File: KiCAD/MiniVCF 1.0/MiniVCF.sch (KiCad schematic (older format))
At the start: 63 parts, among them J10 CV2, J11 CTRL_PANEL_CONN2, J12 MAIN_BOARD_CONN2, J3 AudioIn, J4 CV1, J5 AudioOut, J8 MAIN_BOARD_CONN, J9 CTRL_PANEL_CONN, U1 TL074, U2 TL074

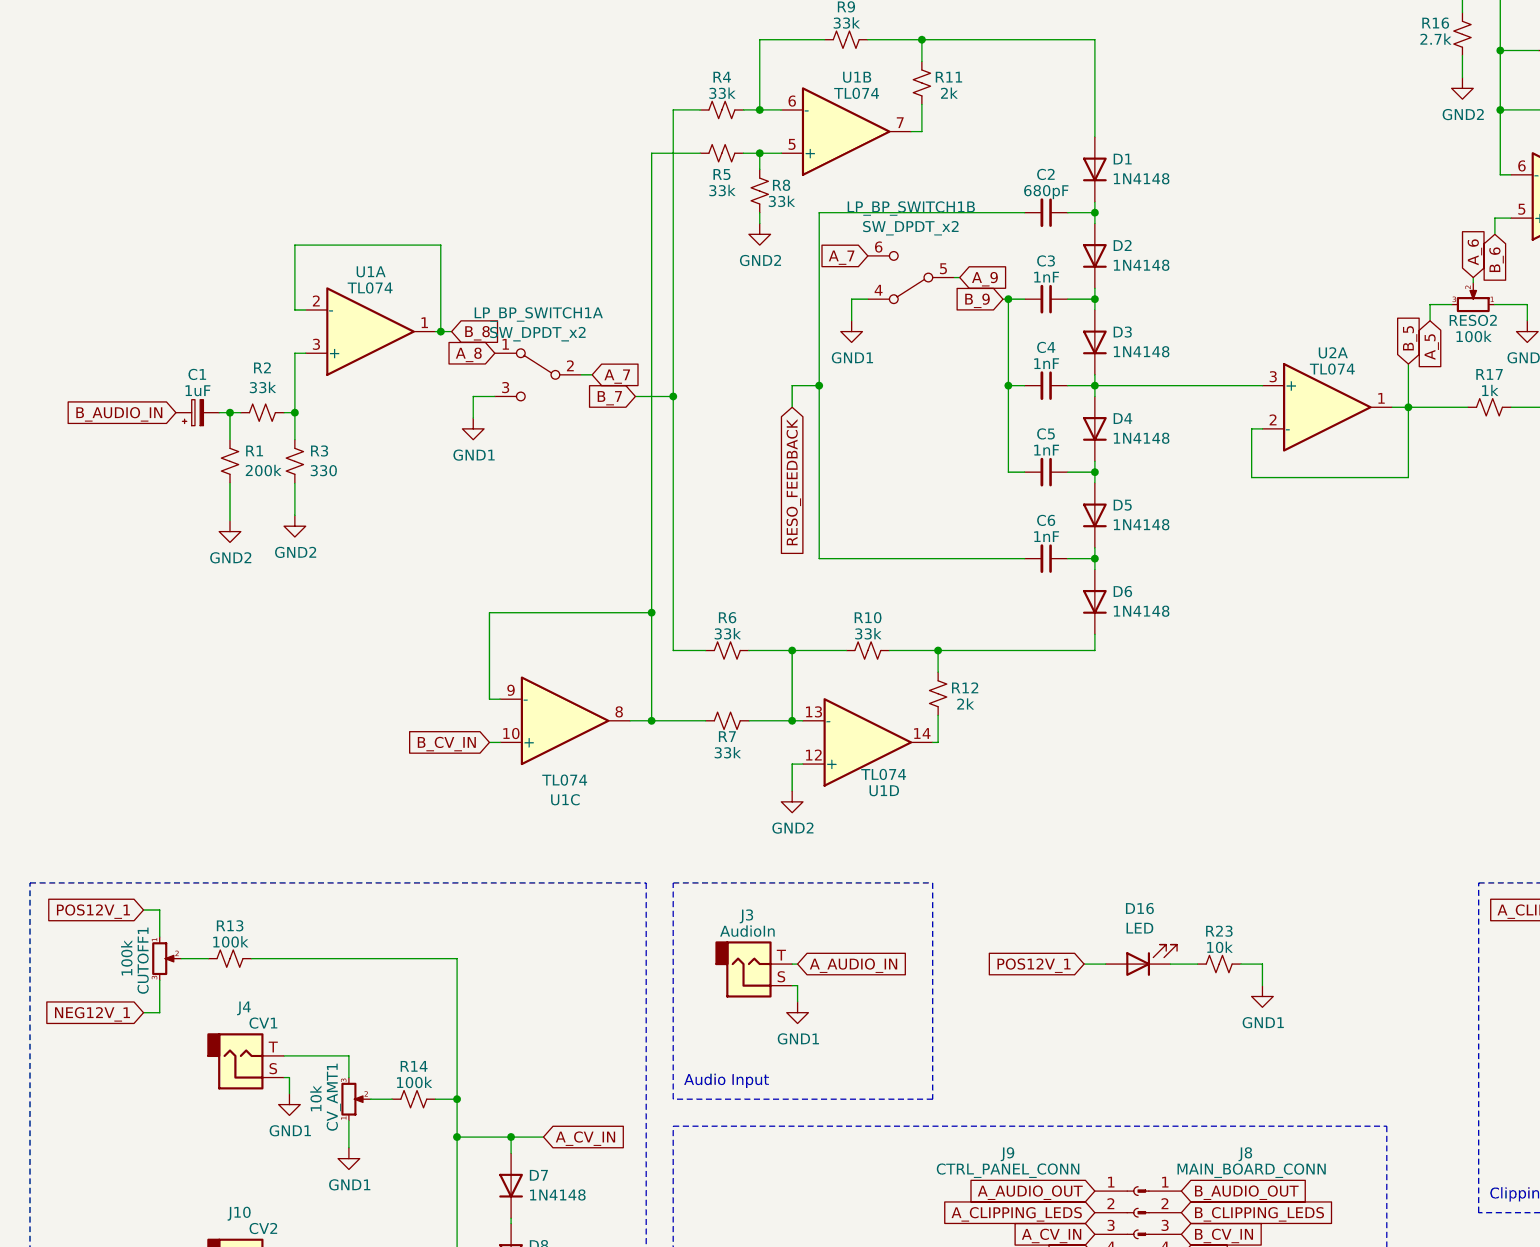
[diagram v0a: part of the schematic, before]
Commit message: Fixed toggle switch connections
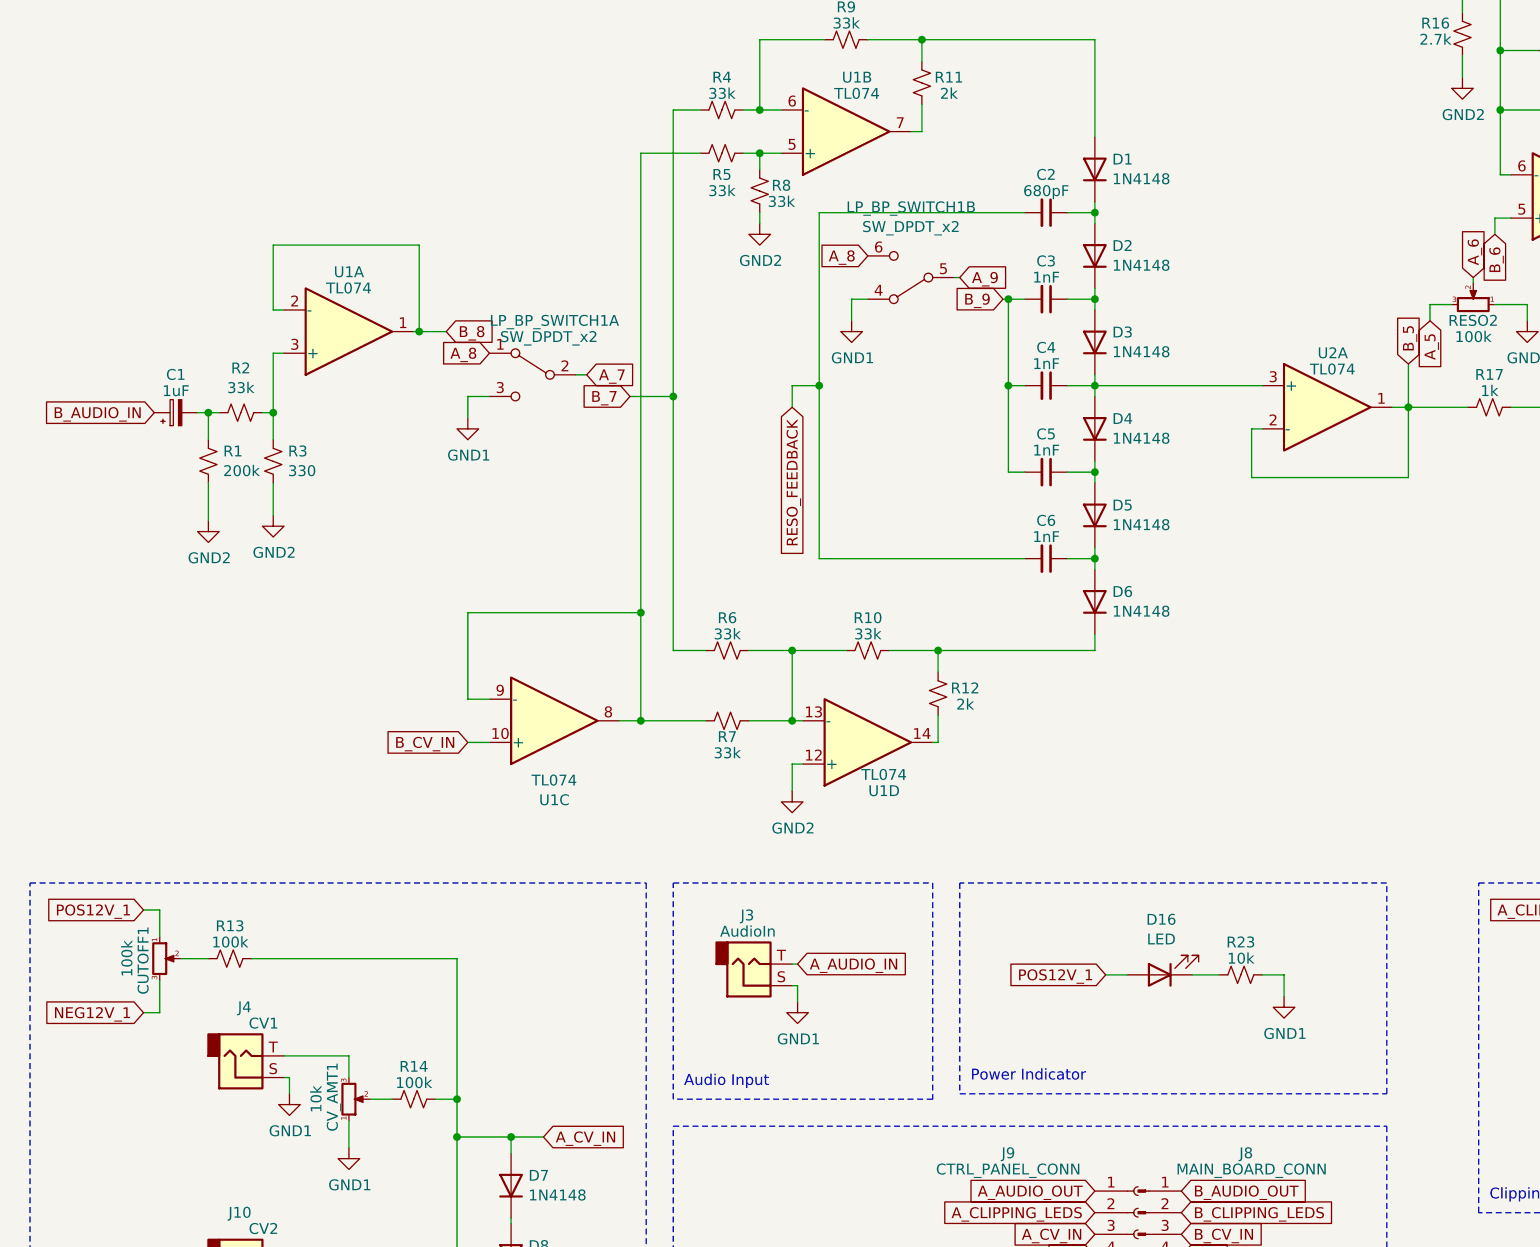
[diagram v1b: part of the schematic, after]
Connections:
- net A_7: no longer LP_BP_SWITCH1.6 (C)
- net A_8: now also LP_BP_SWITCH1.6 (C)
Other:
- note added: "Power Indicator\n"
- moved on the sheet: C1, D16, LP_BP_SWITCH1A, R1, R2, R23, R3, U1A, U1C

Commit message: Added fab files for v1.0
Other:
- moved on the sheet: R16
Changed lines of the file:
@@
 	7550 2275 7550 2350
 Wire Wire Line
-	7425 1375 7425 1675
-Wire Wire Line
-	7425 1675 7475 1675
+	7400 1375 7400 1675
+Wire Wire Line
+	7400 1675 7475 1675
 Wire Wire Line
 	8125 1375 8125 1775
@@
 Wire Wire Line
 	8125 1775 8225 1775
-Wire Wire Line
-	7425 800  7425 1100
-Connection ~ 7425 1375
+Connection ~ 7400 1375
 Wire Wire Line
 	8125 800  8125 1100
 Connection ~ 8125 1375
-Connection ~ 7425 1100
-Wire Wire Line
-	7425 1100 7425 1375
 Connection ~ 8125 1100
 Wire Wire Line
 	8125 1100 8125 1375
 Wire Wire Line
-	7250 800  7250 925
-Connection ~ 7425 800
-Wire Wire Line
-	7250 1125 7250 1225
+	7125 800  7125 925
+Wire Wire Line
+	7125 1125 7125 1200
 Wire Wire Line
 	7800 2450 7800 2750
@@
 L power:GND2 #PWR012
 U 1 1 61F340A5
-P 7250 1225
-F 0 "#PWR012" H 7250 975 50  0001 C CNN
-F 1 "GND2" H 7255 1052 50  0000 C CNN
-F 2 "" H 7250 1225 50  0001 C CNN
-F 3 "" H 7250 1225 50  0001 C CNN
-	1    7250 1225
+P 7125 1200
+F 0 "#PWR012" H 7125 950 50  0001 C CNN
+F 1 "GND2" H 7130 1027 50  0000 C CNN
+F 2 "" H 7125 1200 50  0001 C CNN
+F 3 "" H 7125 1200 50  0001 C CNN
+	1    7125 1200
 	1    0    0    -1
 $EndComp
@@
 Text GLabel 7100 2350 3    50   Input ~ 0
 A_5
-Text GLabel 7300 2150 1    50   Input ~ 0
+Text GLabel 7300 2125 1    50   Input ~ 0
 A_6
 Text GLabel 7000 2550 1    50   Input ~ 0
@@
 Wire Wire Line
 	7000 2550 7000 2750
-Text GLabel 7400 1950 3    50   Input ~ 0
+Text GLabel 7400 1925 3    50   Input ~ 0
 B_6
 Wire Wire Line
-	7300 2150 7300 2175
+	7300 2125 7300 2175
 Wire Wire Line
 	7400 1875 7475 1875
 Wire Wire Line
-	7400 1875 7400 1950
+	7400 1875 7400 1925
 Wire Wire Line
 	7100 2275 7200 2275
@@
 L Device:R_Small_US R16
 U 1 1 62172144
-P 7250 1025
-F 0 "R16" H 7375 975 50  0000 C CNN
-F 1 "2.7k" H 7375 1050 50  0000 C CNN
-F 2 "benjiaomodular:Resistor_L6.3mm_D2.5mm_P7.62mm_Horizontal" H 7250 1025 50  0001 C CNN
-F 3 "~" H 7250 1025 50  0001 C CNN
-	1    7250 1025
+P 7125 1025
+F 0 "R16" H 7250 975 50  0000 C CNN
+F 1 "2.7k" H 7250 1050 50  0000 C CNN
+F 2 "benjiaomodular:Resistor_L6.3mm_D2.5mm_P7.62mm_Horizontal" H 7125 1025 50  0001 C CNN
+F 3 "~" H 7125 1025 50  0001 C CNN
+	1    7125 1025
 	-1   0    0    1
 $EndComp
@@
 	4500 1050 4750 1050
 Wire Wire Line
-	7425 800  7250 800
-Wire Wire Line
 	7900 1100 8125 1100
 Wire Wire Line
@@
 	7475 2750 7800 2750
 Wire Wire Line
-	7650 1375 7425 1375
-Wire Wire Line
-	7600 1100 7425 1100
-Wire Wire Line
-	7600 800  7425 800
+	7650 1375 7400 1375
 Wire Wire Line
 	7400 2275 7550 2275
@@
 Text Notes 4975 5875 0    50   ~ 0
 Power Indicator\n
+Wire Wire Line
+	7600 1100 7400 1100
+Wire Wire Line
+	7400 1100 7400 1375
+Wire Wire Line
+	7600 800  7400 800
+Wire Wire Line
+	7400 800  7125 800
+Connection ~ 7400 800
+Connection ~ 7400 1100
+Wire Wire Line
+	7400 800  7400 1100
 $EndSCHEMATC
